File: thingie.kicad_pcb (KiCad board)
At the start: 4 copper layers, 62.2 x 29.2 mm, 77 parts, among them J1 Conn_01x01_Male, J10 Conn_01x01_Male, J11 Conn_01x01_Male, J12 Conn_01x01_Male, J13 Conn_01x01_Male, J14 Conn_01x01_Male, J15 Conn_01x01_Male, J16 Conn_01x01_Male, J17 Conn_01x01_Male, J18 Conn_01x01_Male, J19 Conn_01x01_Male, J2 Conn_01x01_Male, J20 Conn_01x01_Male, J21 Conn_01x01_Male, J22 Conn_01x01_Male, J23 Conn_01x01_Male, J24 Conn_01x01_Male, J25 Conn_01x01_Male, J26 Conn_01x01_Male, J27 Conn_01x01_Male, J28 Conn_01x01_Male, J29 Conn_01x01_Male, J3 Conn_01x01_Male, J30 Conn_01x01_Male, J31 Conn_01x01_Male, J32 Conn_01x01_Male, J33 Conn_01x01_Male, J34 Conn_01x01_Male, J35 Conn_01x01_Male, J36 AudioJack4, J37 Conn_01x01_Male, J38 Conn_01x01_Male, J39 Conn_01x01_Male, J4 Conn_01x01_Male, J40 Conn_01x01_Male, J41 Conn_01x01_Male, J5 Conn_01x01_Male, J6 Conn_01x01_Male, J7 Conn_01x01_Male, J8 Conn_01x12, J9 Conn_01x01_Male, Q1 Q_NPN_BEC, SW13 SW_Push, SW14 SW_Push, U1 buttonarray, U2 SGTL5000XNAA3, U3 AP7313, U4 LTC1733, U5 DS2782, U6 TPS2116

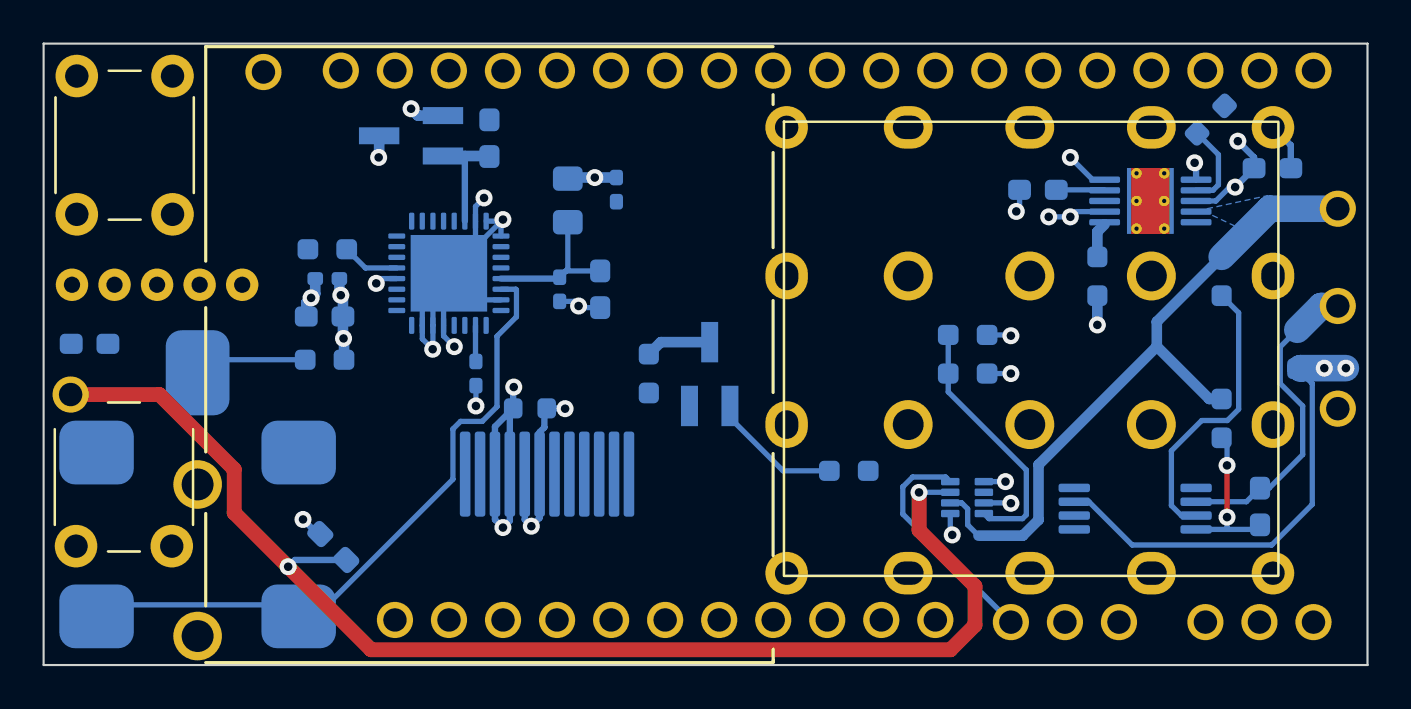
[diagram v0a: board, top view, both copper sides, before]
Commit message: start modifying the schematic in preperation to add an RP2350
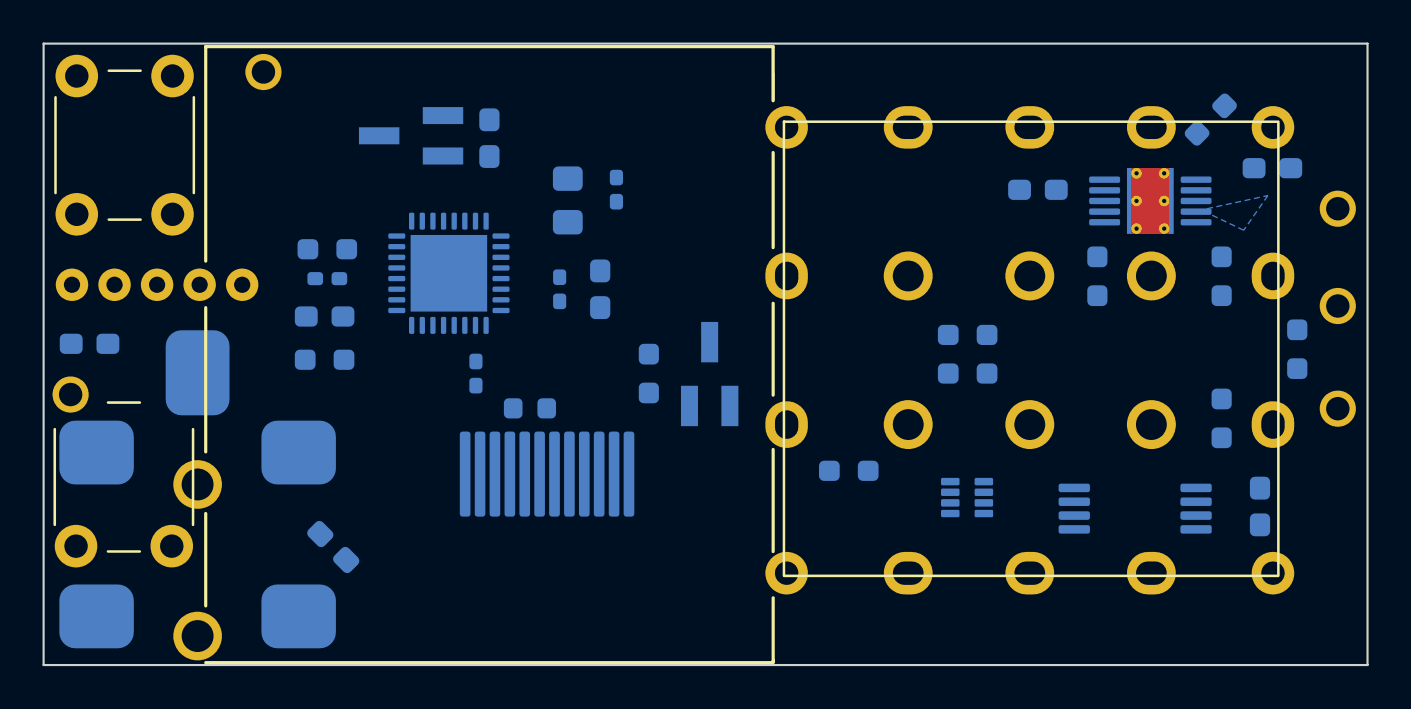
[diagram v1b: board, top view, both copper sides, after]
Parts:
- removed J1, J11, J12, J13, J14, J15, J16, J17, J18, J19, J2, J20, J21, J22, J23, J24, J25, J26, J27, J28, J29, J30, J31, J32, J33, J34, J35, J39, J4, J40, J41, J5, J6, J7, J9: Conn_01x01_Male, custom_footprints:hole
- removed the J10 at (53.1, 14.7)
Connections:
- net Net-(J40-Pin_1) renamed /CHG_ON
- C10 pad 2: GNDREF -> GND1
- C11 pad 2: GNDREF -> GND1
- R1 pad 2: GNDREF -> GND1
- R9 pad 2: GNDREF -> GND1
- SW13 pad 1: GNDREF -> unconnected-(SW13-Pad1)
- SW13 pad 2: Net-(J1-Pin_1) -> GNDREF
- SW14 pad 1: GNDREF -> unconnected-(SW14-Pad1)
- SW14 pad 2: Net-(J12-Pin_1) -> GNDREF
- U1 pad 1: Net-(J24-Pin_1) -> unconnected-(U1-Pad1)
- U1 pad 10: Net-(J15-Pin_1) -> unconnected-(U1-Pad10)
- U1 pad 11: Net-(J14-Pin_1) -> unconnected-(U1-Pad11)
- U1 pad 12: Net-(J13-Pin_1) -> unconnected-(U1-Pad12)
- U1 pad 2: Net-(J23-Pin_1) -> unconnected-(U1-Pad2)
- U1 pad 3: Net-(J22-Pin_1) -> unconnected-(U1-Pad3)
- U1 pad 4: Net-(J21-Pin_1) -> unconnected-(U1-Pad4)
- U1 pad 5: Net-(J20-Pin_1) -> unconnected-(U1-Pad5)
- U1 pad 6: Net-(J19-Pin_1) -> unconnected-(U1-Pad6)
- U1 pad 7: Net-(J17-Pin_1) -> unconnected-(U1-Pad7)
- U1 pad 8: Net-(J18-Pin_1) -> unconnected-(U1-Pad8)
- U1 pad 9: Net-(J16-Pin_1) -> unconnected-(U1-Pad9)
- U4 pad 3: Net-(J41-Pin_1) -> /CHG_FAULT
- U4 pad 5: GNDREF -> GND1
- U4 pad 6: GNDREF -> GND1
- U5 pad 7: GNDREF -> GND1
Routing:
- net GNDREF: track 70.7 -> 0.00 mm, vias 18 -> 0
- net VCC: track 60.8 -> 0.00 mm, vias 2 -> 0
- net /LEFT: track 33.2 -> 0.00 mm
- net +BATT: track 31.9 -> 0.00 mm
- net +3V3: track 21.8 -> 0.00 mm, vias 7 -> 0
- net /CELL-: track 14.9 -> 0.00 mm
- net Net-(U5-VIN): track 13.6 -> 0.00 mm
- net +5V: track 12.5 -> 0.00 mm, vias 8 -> 0
- net Net-(U6-PR1): track 12.1 -> 0.00 mm
- net /PWR_SRC: track 11.0 -> 0.00 mm
- net Net-(U2-VDDA): track 7.91 -> 0.00 mm
- net Net-(U5-VDD): track 7.50 -> 0.00 mm, vias 2 -> 0
- net Net-(Q1-B): track 6.26 -> 0.00 mm
- net /BUTTON_SENSE: track 5.31 -> 0.00 mm
- net /+1V8: track 5.26 -> 0.00 mm
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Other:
- board text removed: "3V3"
- board text removed: "GND"
- board text removed: "LCD_BL"
- board text removed: "LCD_DC"
- board text removed: "LRCLK"
- board text removed: "MCLK"
- board text removed: "SCL"
- board text removed: "SDA"
- board text removed: "SENSE"

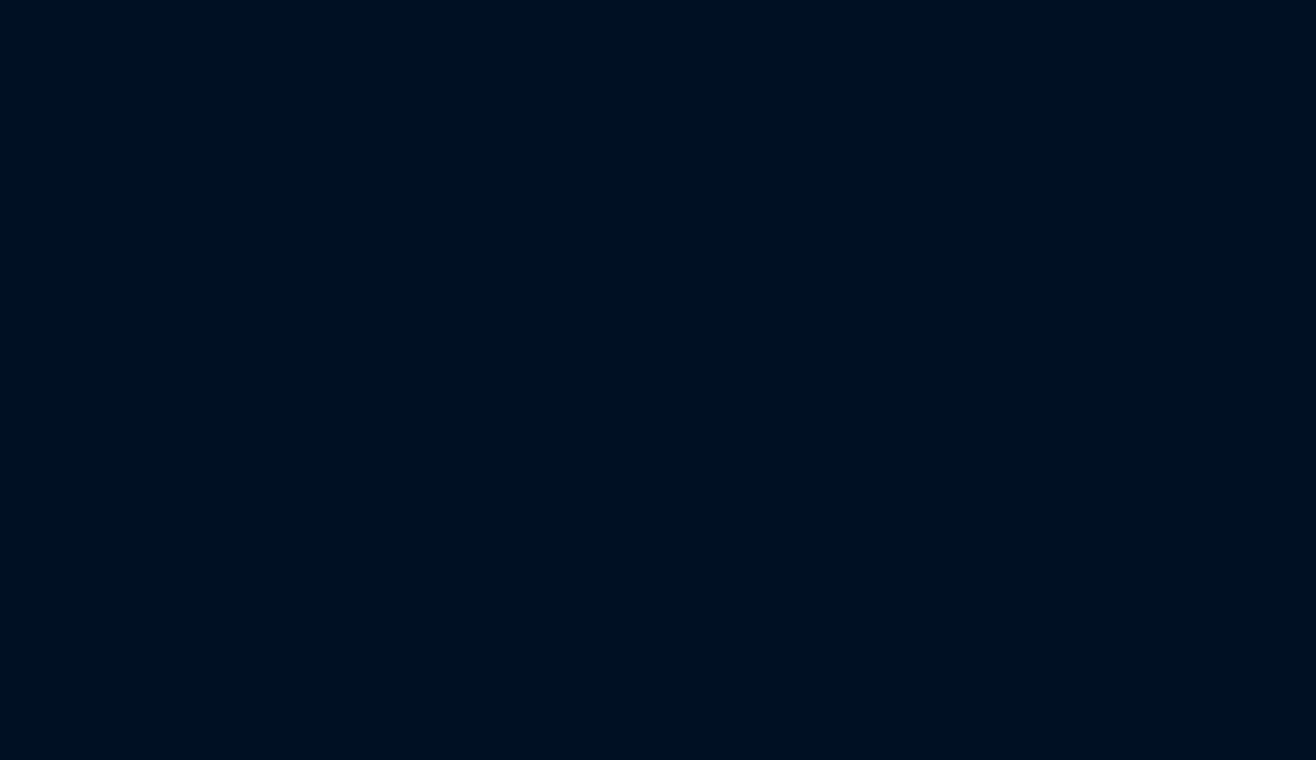
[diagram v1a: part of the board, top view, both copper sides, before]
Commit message: new µc schematic - it ain't all fitting on the PCB. Hmph.
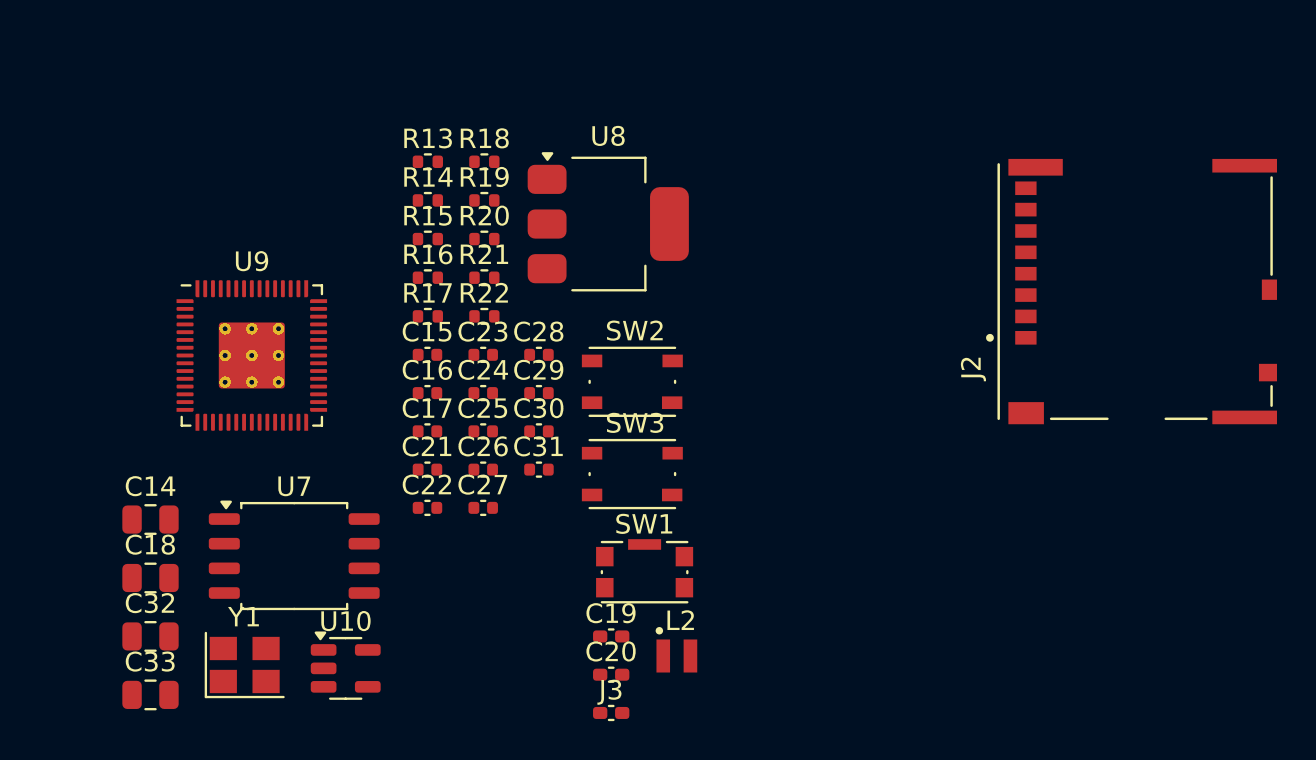
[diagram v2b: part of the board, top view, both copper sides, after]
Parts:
- added C14: 10u, Capacitor_SMD:C_0805_2012Metric, F.Cu at (31.9, 74.0)
- added C15: 15p, Capacitor_SMD:C_0402_1005Metric, F.Cu at (46.1, 65.5)
- added C16: 15p, Capacitor_SMD:C_0402_1005Metric, F.Cu at (46.1, 67.5)
- added C17: 100n, Capacitor_SMD:C_0402_1005Metric, F.Cu at (46.1, 69.5)
- added C18: 10u, Capacitor_SMD:C_0805_2012Metric, F.Cu at (31.9, 77.0)
- added C19: 4.7u, Capacitor_SMD:C_0402_1005Metric_Pad0.74x0.62mm_HandSolder, F.Cu at (55.6, 80.0)
- added C20: 4.7u, Capacitor_SMD:C_0402_1005Metric_Pad0.74x0.62mm_HandSolder, F.Cu at (55.6, 82.0)
- added C21: 100n, Capacitor_SMD:C_0402_1005Metric, F.Cu at (46.1, 71.4)
- added C22: 4.7u, Capacitor_SMD:C_0402_1005Metric, F.Cu at (46.1, 73.4)
- added C23: 4.7u, Capacitor_SMD:C_0402_1005Metric, F.Cu at (49.0, 65.5)
- added C24: 100n, Capacitor_SMD:C_0402_1005Metric, F.Cu at (49.0, 67.5)
- added C25: 100n, Capacitor_SMD:C_0402_1005Metric, F.Cu at (49.0, 69.5)
- added C26: 100n, Capacitor_SMD:C_0402_1005Metric, F.Cu at (49.0, 71.4)
- added C27: 100n, Capacitor_SMD:C_0402_1005Metric, F.Cu at (49.0, 73.4)
- added C28: 100n, Capacitor_SMD:C_0402_1005Metric, F.Cu at (51.9, 65.5)
- added C29: 100n, Capacitor_SMD:C_0402_1005Metric, F.Cu at (51.9, 67.5)
- added C30: 100n, Capacitor_SMD:C_0402_1005Metric, F.Cu at (51.9, 69.5)
- added C31: 100n, Capacitor_SMD:C_0402_1005Metric, F.Cu at (51.9, 71.4)
- added C32: 10u, Capacitor_SMD:C_0805_2012Metric, F.Cu at (31.9, 80.0)
- added C33: 10u, Capacitor_SMD:C_0805_2012Metric, F.Cu at (31.9, 83.0)
- added J2: Micro_SD_Card_Det, CM4IO:SDCARD_MOLEX_503398-1892, F.Cu at (82.6, 62.3)
- added J3: USB_C_Receptacle_USB2.0_14P, Capacitor_SMD:C_0402_1005Metric_Pad0.74x0.62mm_HandSolder, F.Cu at (55.6, 84.0)
- added L2: 3.3u, RP2350_60QFN_minimal:L_pol_2016, F.Cu at (59.0, 81.0)
- added R13: DNF, Resistor_SMD:R_0402_1005Metric, F.Cu at (46.2, 55.6)
- added R14: 0, Resistor_SMD:R_0402_1005Metric, F.Cu at (46.2, 57.6)
- added R15: DNF, Resistor_SMD:R_0402_1005Metric, F.Cu at (46.2, 59.6)
- added R16: 1k, Resistor_SMD:R_0402_1005Metric, F.Cu at (46.2, 61.5)
- added R17: 1k, Resistor_SMD:R_0402_1005Metric, F.Cu at (46.2, 63.5)
- added R18: 33, Resistor_SMD:R_0402_1005Metric, F.Cu at (49.1, 55.6)
- added R19: 1k, Resistor_SMD:R_0402_1005Metric, F.Cu at (49.1, 57.6)
- added R20: 27, Resistor_SMD:R_0402_1005Metric, F.Cu at (49.1, 59.6)
- added R21: 27, Resistor_SMD:R_0402_1005Metric, F.Cu at (49.1, 61.5)
- added R22: 12K 1%, Resistor_SMD:R_0402_1005Metric, F.Cu at (49.1, 63.5)
- added SW1: SW_SPST, Button_Switch_SMD:SW_Push_1P1T-SH_NO_CK_KMR2xxG, F.Cu at (57.3, 76.7)
- added SW2: SW_Push, Button_Switch_SMD:SW_Push_1P1T_NO_Vertical_Wuerth_434133025816, F.Cu at (56.7, 66.9)
- added SW3: SW_Push, Button_Switch_SMD:SW_Push_1P1T_NO_Vertical_Wuerth_434133025816, F.Cu at (56.7, 71.7)
- added U10: RT9742GGJ5, Package_TO_SOT_SMD:SOT-23-5, F.Cu at (41.9, 81.7)
- added U7: W25Q128JVS, Package_SO:SOIC-8_5.23x5.23mm_P1.27mm, F.Cu at (39.3, 75.9)
- added U8: NCP1117-3.3_SOT223, Package_TO_SOT_SMD:SOT-223-3_TabPin2, F.Cu at (55.5, 58.8)
- added U9: RP2350_60QFN, RP2350_60QFN_minimal:RP2350-QFN-60-1EP_7x7_P0.4mm_EP3.4x3.4mm_ThermalVias, F.Cu at (37.1, 65.6)
- added Y1: ABM8-272-T3, Crystal:Crystal_SMD_3225-4Pin_3.2x2.5mm, F.Cu at (36.7, 81.5)
